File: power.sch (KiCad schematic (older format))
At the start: 21 parts

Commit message: Add power switch
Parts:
- added SW?: SPST, symbol SPST
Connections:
- net +BATT: now also SW?.1; no longer Q?.S
- new net: Q?.S, SW?.2
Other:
- moved on the sheet: C?, D?, Q?, R?, U?
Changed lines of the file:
@@
 L MOS_P Q?
 U 1 1 54E64290
-P 2200 3900
-F 0 "Q?" H 2200 4090 60  0000 R CNN
-F 1 "MOS_P" H 2200 3720 60  0000 R CNN
-F 2 "" H 2200 3900 60  0000 C CNN
-F 3 "" H 2200 3900 60  0000 C CNN
-	1    2200 3900
+P 2600 3900
+F 0 "Q?" H 2600 4090 60  0000 R CNN
+F 1 "MOS_P" H 2600 3720 60  0000 R CNN
+F 2 "" H 2600 3900 60  0000 C CNN
+F 3 "" H 2600 3900 60  0000 C CNN
+	1    2600 3900
 	0    1    1    0
 $EndComp
@@
 L +BATT #PWR?
 U 1 1 54E64297
-P 1600 3900
-F 0 "#PWR?" H 1600 3850 20  0001 C CNN
-F 1 "+BATT" H 1600 4000 30  0000 C CNN
-F 2 "" H 1600 3900 60  0000 C CNN
-F 3 "" H 1600 3900 60  0000 C CNN
-	1    1600 3900
+P 1100 3900
+F 0 "#PWR?" H 1100 3850 20  0001 C CNN
+F 1 "+BATT" H 1100 4000 30  0000 C CNN
+F 2 "" H 1100 3900 60  0000 C CNN
+F 3 "" H 1100 3900 60  0000 C CNN
+	1    1100 3900
 	1    0    0    -1
 $EndComp
@@
 L CP C?
 U 1 1 54E6429D
-P 2800 4300
-F 0 "C?" H 2850 4400 40  0000 L CNN
-F 1 "4.7uF" H 2850 4200 40  0000 L CNN
-F 2 "" H 2900 4150 30  0000 C CNN
-F 3 "" H 2800 4300 300 0000 C CNN
-	1    2800 4300
+P 3200 4300
+F 0 "C?" H 3250 4400 40  0000 L CNN
+F 1 "4.7uF" H 3250 4200 40  0000 L CNN
+F 2 "" H 3300 4150 30  0000 C CNN
+F 3 "" H 3200 4300 300 0000 C CNN
+	1    3200 4300
 	1    0    0    -1
 $EndComp
@@
 L DIODESCH D?
 U 1 1 54E642A4
-P 2600 3500
-F 0 "D?" H 2600 3600 40  0000 C CNN
-F 1 "DIODESCH" H 2600 3400 40  0000 C CNN
-F 2 "" H 2600 3500 60  0000 C CNN
-F 3 "" H 2600 3500 60  0000 C CNN
-	1    2600 3500
+P 3000 3500
+F 0 "D?" H 3000 3600 40  0000 C CNN
+F 1 "DIODESCH" H 3000 3400 40  0000 C CNN
+F 2 "" H 3000 3500 60  0000 C CNN
+F 3 "" H 3000 3500 60  0000 C CNN
+	1    3000 3500
 	1    0    0    -1
 $EndComp
@@
 L MCP1700 U?
 U 1 1 54E642AB
-P 3500 4050
-F 0 "U?" H 3650 3854 60  0000 C CNN
-F 1 "MCP1700" H 3500 4250 60  0000 C CNN
-F 2 "" H 3500 4050 60  0000 C CNN
-F 3 "" H 3500 4050 60  0000 C CNN
-	1    3500 4050
+P 3900 4050
+F 0 "U?" H 4050 3854 60  0000 C CNN
+F 1 "MCP1700" H 3900 4250 60  0000 C CNN
+F 2 "" H 3900 4050 60  0000 C CNN
+F 3 "" H 3900 4050 60  0000 C CNN
+	1    3900 4050
 	1    0    0    -1
 $EndComp
@@
 L VCC #PWR?
 U 1 1 54E642B2
-P 4200 3900
-F 0 "#PWR?" H 4200 4000 30  0001 C CNN
-F 1 "VCC" H 4200 4000 30  0000 C CNN
-F 2 "" H 4200 3900 60  0000 C CNN
-F 3 "" H 4200 3900 60  0000 C CNN
-	1    4200 3900
+P 4600 3900
+F 0 "#PWR?" H 4600 4000 30  0001 C CNN
+F 1 "VCC" H 4600 4000 30  0000 C CNN
+F 2 "" H 4600 3900 60  0000 C CNN
+F 3 "" H 4600 3900 60  0000 C CNN
+	1    4600 3900
 	1    0    0    -1
 $EndComp
 Wire Wire Line
-	2400 4000 3100 4000
+	2800 4000 3500 4000
 Wire Wire Line
-	2800 3500 2800 4100
-Connection ~ 2800 4000
+	3200 3500 3200 4100
+Connection ~ 3200 4000
 Wire Wire Line
-	1600 3900 1600 4000
+	1100 3900 1100 4000
 Wire Wire Line
-	1600 4000 2000 4000
+	2600 3700 2600 3500
 Wire Wire Line
-	2200 3700 2200 3500
-Wire Wire Line
-	1300 3500 2400 3500
+	800  3500 2800 3500
 $Comp
 L +5V #PWR?
 U 1 1 54E642BF
-P 1600 3400
-F 0 "#PWR?" H 1600 3490 20  0001 C CNN
-F 1 "+5V" H 1600 3490 30  0000 C CNN
-F 2 "" H 1600 3400 60  0000 C CNN
-F 3 "" H 1600 3400 60  0000 C CNN
-	1    1600 3400
+P 2000 3400
+F 0 "#PWR?" H 2000 3490 20  0001 C CNN
+F 1 "+5V" H 2000 3490 30  0000 C CNN
+F 2 "" H 2000 3400 60  0000 C CNN
+F 3 "" H 2000 3400 60  0000 C CNN
+	1    2000 3400
 	1    0    0    -1
 $EndComp
 Wire Wire Line
-	1600 3400 1600 3500
-Connection ~ 2200 3500
+	2000 3400 2000 3500
+Connection ~ 2600 3500
 Wire Wire Line
-	3900 4000 4200 4000
+	4300 4000 4600 4000
 Wire Wire Line
-	4200 3900 4200 4100
+	4600 3900 4600 4100
 $Comp
 L GND #PWR?
 U 1 1 54E642C9
-P 3500 4600
-F 0 "#PWR?" H 3500 4600 30  0001 C CNN
-F 1 "GND" H 3500 4530 30  0001 C CNN
-F 2 "" H 3500 4600 60  0000 C CNN
-F 3 "" H 3500 4600 60  0000 C CNN
-	1    3500 4600
+P 3900 4600
+F 0 "#PWR?" H 3900 4600 30  0001 C CNN
+F 1 "GND" H 3900 4530 30  0001 C CNN
+F 2 "" H 3900 4600 60  0000 C CNN
+F 3 "" H 3900 4600 60  0000 C CNN
+	1    3900 4600
 	1    0    0    -1
 $EndComp
 Wire Wire Line
-	1300 4500 4200 4500
+	800  4500 4600 4500
 Wire Wire Line
-	3500 4300 3500 4600
-Connection ~ 3500 4500
+	3900 4300 3900 4600
+Connection ~ 3900 4500
 $Comp
 L R R?
 U 1 1 54E642D2
-P 1300 4050
-F 0 "R?" V 1380 4050 40  0000 C CNN
-F 1 "15k" V 1307 4051 40  0000 C CNN
-F 2 "" V 1230 4050 30  0000 C CNN
-F 3 "" H 1300 4050 30  0000 C CNN
-	1    1300 4050
+P 800 4050
+F 0 "R?" V 880 4050 40  0000 C CNN
+F 1 "15k" V 807 4051 40  0000 C CNN
+F 2 "" V 730 4050 30  0000 C CNN
+F 3 "" H 800 4050 30  0000 C CNN
+	1    800  4050
 	-1   0    0    1
 $EndComp
 Wire Wire Line
-	1300 3800 1300 3500
-Connection ~ 1600 3500
+	800  3800 800  3500
+Connection ~ 2000 3500
 Wire Wire Line
-	1300 4300 1300 4500
-Connection ~ 2800 4500
+	800  4300 800  4500
+Connection ~ 3200 4500
 $Comp
 L CP C?
 U 1 1 54E642DD
-P 4200 4300
-F 0 "C?" H 4250 4400 40  0000 L CNN
-F 1 "4.7uF" H 4250 4200 40  0000 L CNN
-F 2 "" H 4300 4150 30  0000 C CNN
-F 3 "" H 4200 4300 300 0000 C CNN
-	1    4200 4300
+P 4600 4300
+F 0 "C?" H 4650 4400 40  0000 L CNN
+F 1 "4.7uF" H 4650 4200 40  0000 L CNN
+F 2 "" H 4700 4150 30  0000 C CNN
+F 3 "" H 4600 4300 300 0000 C CNN
+	1    4600 4300
 	1    0    0    -1
 $EndComp
-Connection ~ 4200 4000
+Connection ~ 4600 4000
+$Comp
+L SPST SW?
+U 1 1 54E81B6B
+P 1700 4000
+F 0 "SW?" H 1700 4100 70  0000 C CNN
+F 1 "SPST" H 1700 3900 70  0000 C CNN
+F 2 "" H 1700 4000 60  0000 C CNN
+F 3 "" H 1700 4000 60  0000 C CNN
+	1    1700 4000
+	1    0    0    -1
+$EndComp
+Wire Wire Line
+	1100 4000 1200 4000
+Wire Wire Line
+	2200 4000 2400 4000
 $EndSCHEMATC

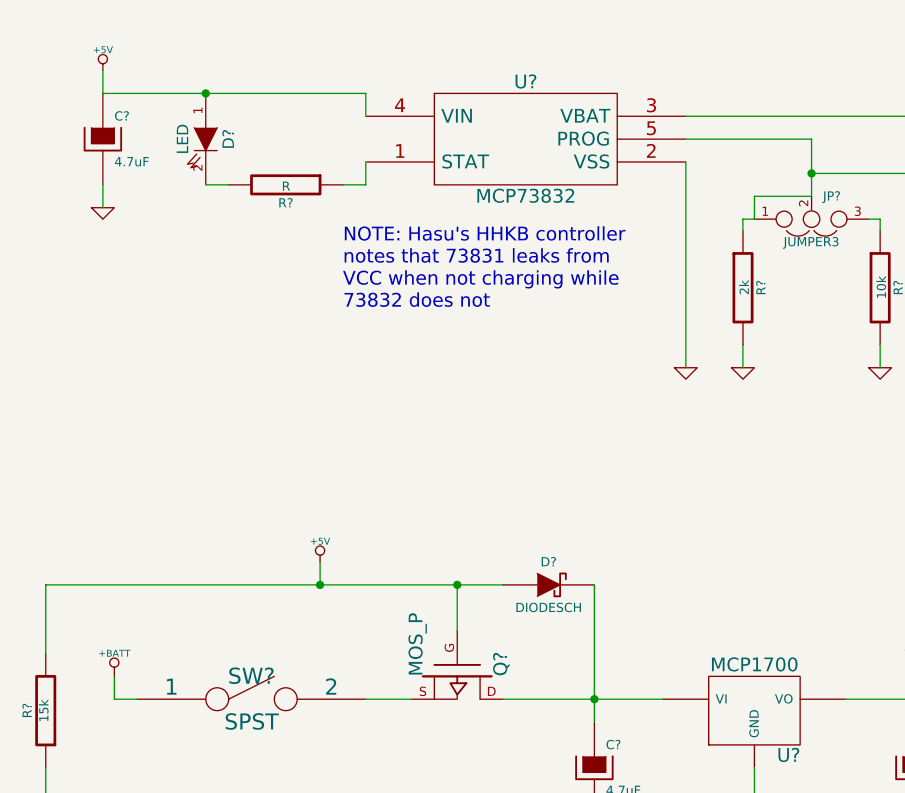
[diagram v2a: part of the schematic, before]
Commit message: Add connections from battery monitoring circuitry to 32u4
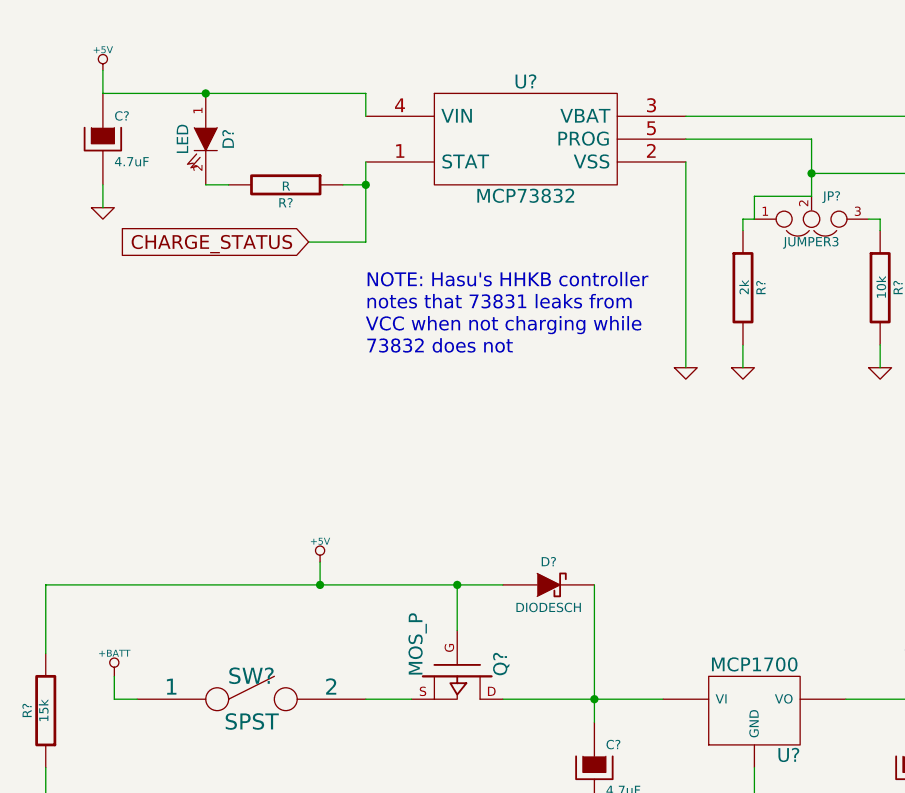
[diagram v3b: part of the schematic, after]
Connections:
- net CHARGE_STATUS: now reaches R?.1, U?.1 (STAT)
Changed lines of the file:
@@
 	2100 1750 2200 1750
 Wire Wire Line
-	2200 1750 2200 1650
+	2200 1650 2200 2000
 Wire Wire Line
 	2200 1350 2200 1450
@@
 Wire Wire Line
 	5250 1650 5250 2550
-Text Notes 2100 2300 0    60   ~ 0
+Text Notes 2200 2500 0    60   ~ 0
 NOTE: Hasu's HHKB controller\nnotes that 73831 leaks from\nVCC when not charging while\n73832 does not
 $Comp
@@
 	1100 3900 1100 4000
 Wire Wire Line
-	2600 3700 2600 3500
+	2600 3500 2600 3700
 Wire Wire Line
 	800  3500 2800 3500
@@
 Wire Wire Line
 	2200 4000 2400 4000
+Text GLabel 1950 2000 0    60   Input ~ 0
+CHARGE_STATUS
+Wire Wire Line
+	2200 2000 1950 2000
+Connection ~ 2200 1750
 $EndSCHEMATC

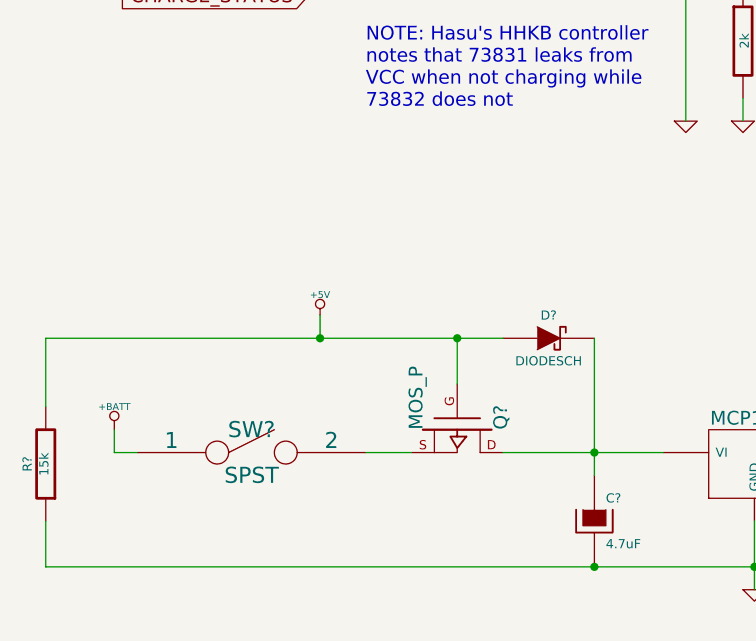
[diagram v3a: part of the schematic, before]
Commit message: Change voltage source auto switch over circuitry to match Hasu's
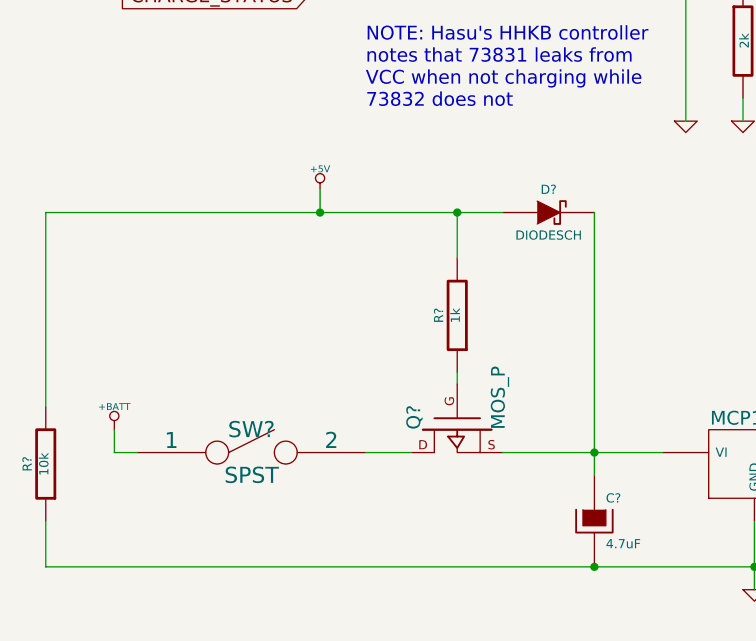
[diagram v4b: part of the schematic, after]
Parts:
- added R?: 1k, symbol R
- R?: value 15k -> 10k
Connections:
- net +5V: now also R?.2; no longer Q?.G
- net at C?.1, D?.2 (K), U?.VI: now also Q?.S; no longer Q?.D
- net at SW?.2: now also Q?.D; no longer Q?.S
- new net: Q?.G, R?.1
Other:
- moved on the sheet: D?
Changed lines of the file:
@@
 F 3 "" H 2600 3900 60  0000 C CNN
 	1    2600 3900
-	0    1    1    0
+	0    -1   1    0
 $EndComp
 $Comp
@@
 L DIODESCH D?
 U 1 1 54E642A4
-P 3000 3500
-F 0 "D?" H 3000 3600 40  0000 C CNN
-F 1 "DIODESCH" H 3000 3400 40  0000 C CNN
-F 2 "" H 3000 3500 60  0000 C CNN
-F 3 "" H 3000 3500 60  0000 C CNN
-	1    3000 3500
+P 3000 2950
+F 0 "D?" H 3000 3050 40  0000 C CNN
+F 1 "DIODESCH" H 3000 2850 40  0000 C CNN
+F 2 "" H 3000 2950 60  0000 C CNN
+F 3 "" H 3000 2950 60  0000 C CNN
+	1    3000 2950
 	1    0    0    -1
 $EndComp
@@
 	2800 4000 3500 4000
 Wire Wire Line
-	3200 3500 3200 4100
+	3200 2950 3200 4100
 Connection ~ 3200 4000
 Wire Wire Line
 	1100 3900 1100 4000
 Wire Wire Line
-	2600 3500 2600 3700
+	2600 2950 2600 3150
 Wire Wire Line
-	800  3500 2800 3500
+	800  2950 2800 2950
 $Comp
 L +5V #PWR?
 U 1 1 54E642BF
-P 2000 3400
-F 0 "#PWR?" H 2000 3490 20  0001 C CNN
-F 1 "+5V" H 2000 3490 30  0000 C CNN
-F 2 "" H 2000 3400 60  0000 C CNN
-F 3 "" H 2000 3400 60  0000 C CNN
-	1    2000 3400
+P 2000 2850
+F 0 "#PWR?" H 2000 2940 20  0001 C CNN
+F 1 "+5V" H 2000 2940 30  0000 C CNN
+F 2 "" H 2000 2850 60  0000 C CNN
+F 3 "" H 2000 2850 60  0000 C CNN
+	1    2000 2850
 	1    0    0    -1
 $EndComp
 Wire Wire Line
-	2000 3400 2000 3500
-Connection ~ 2600 3500
+	2000 2850 2000 2950
+Connection ~ 2600 2950
 Wire Wire Line
 	4300 4000 4600 4000
@@
 P 800 4050
 F 0 "R?" V 880 4050 40  0000 C CNN
-F 1 "15k" V 807 4051 40  0000 C CNN
+F 1 "10k" V 807 4051 40  0000 C CNN
 F 2 "" V 730 4050 30  0000 C CNN
 F 3 "" H 800 4050 30  0000 C CNN
@@
 $EndComp
 Wire Wire Line
-	800  3800 800  3500
-Connection ~ 2000 3500
+	800  2950 800  3800
+Connection ~ 2000 2950
 Wire Wire Line
 	800  4300 800  4500
@@
 	2200 2000 1950 2000
 Connection ~ 2200 1750
+$Comp
+L R R?
+U 1 1 54E977E3
+P 2600 3400
+F 0 "R?" V 2680 3400 40  0000 C CNN
+F 1 "1k" V 2607 3401 40  0000 C CNN
+F 2 "" V 2530 3400 30  0000 C CNN
+F 3 "" H 2600 3400 30  0000 C CNN
+	1    2600 3400
+	-1   0    0    1
+$EndComp
+Wire Wire Line
+	2600 3650 2600 3700
 $EndSCHEMATC
